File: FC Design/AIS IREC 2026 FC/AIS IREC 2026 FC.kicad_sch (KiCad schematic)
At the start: 52 parts, among them IC1 ADXL314WBCPZ-RL, IC2 MT29F8G08ABACAWP-IT_C_TR, J1 USB4216-03-A, J2 EBAA-02-C, J3 Conn_01x08, J4 EBAA-02-C, J5 EBAA-02-C, J6 USB4216-03-A, Q1 MMBT3906-TP, Q2 DMN2008LFU-7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

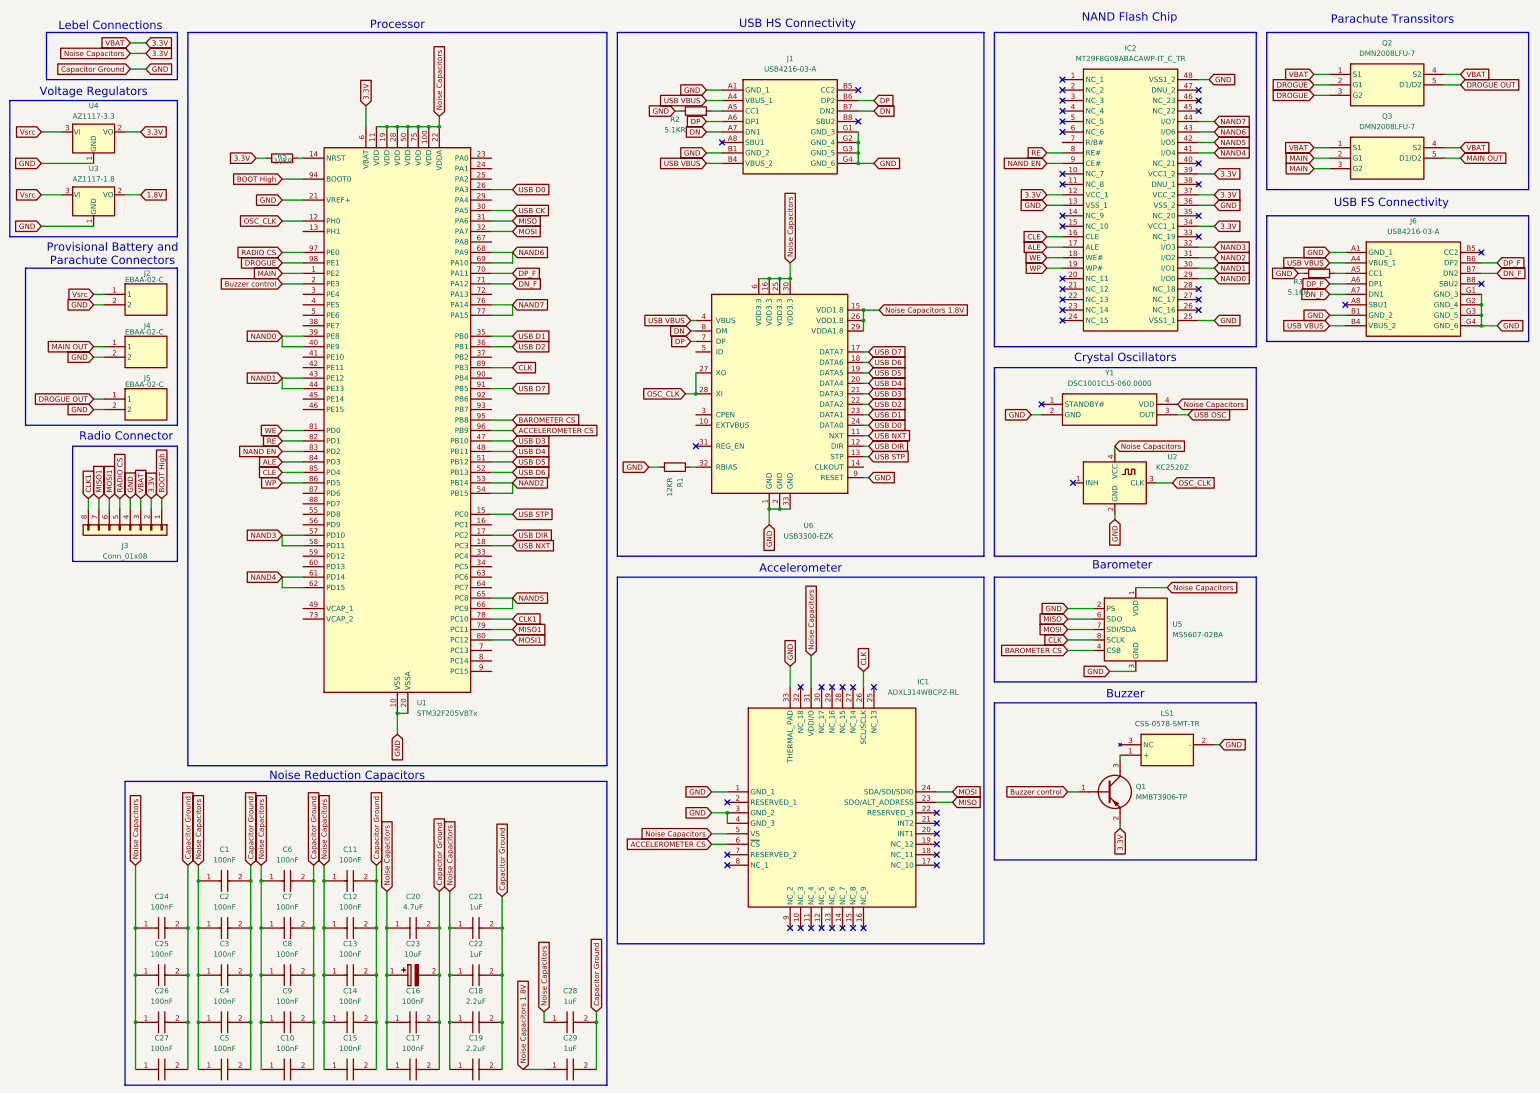
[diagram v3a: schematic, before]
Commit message: Component placement done for pcb
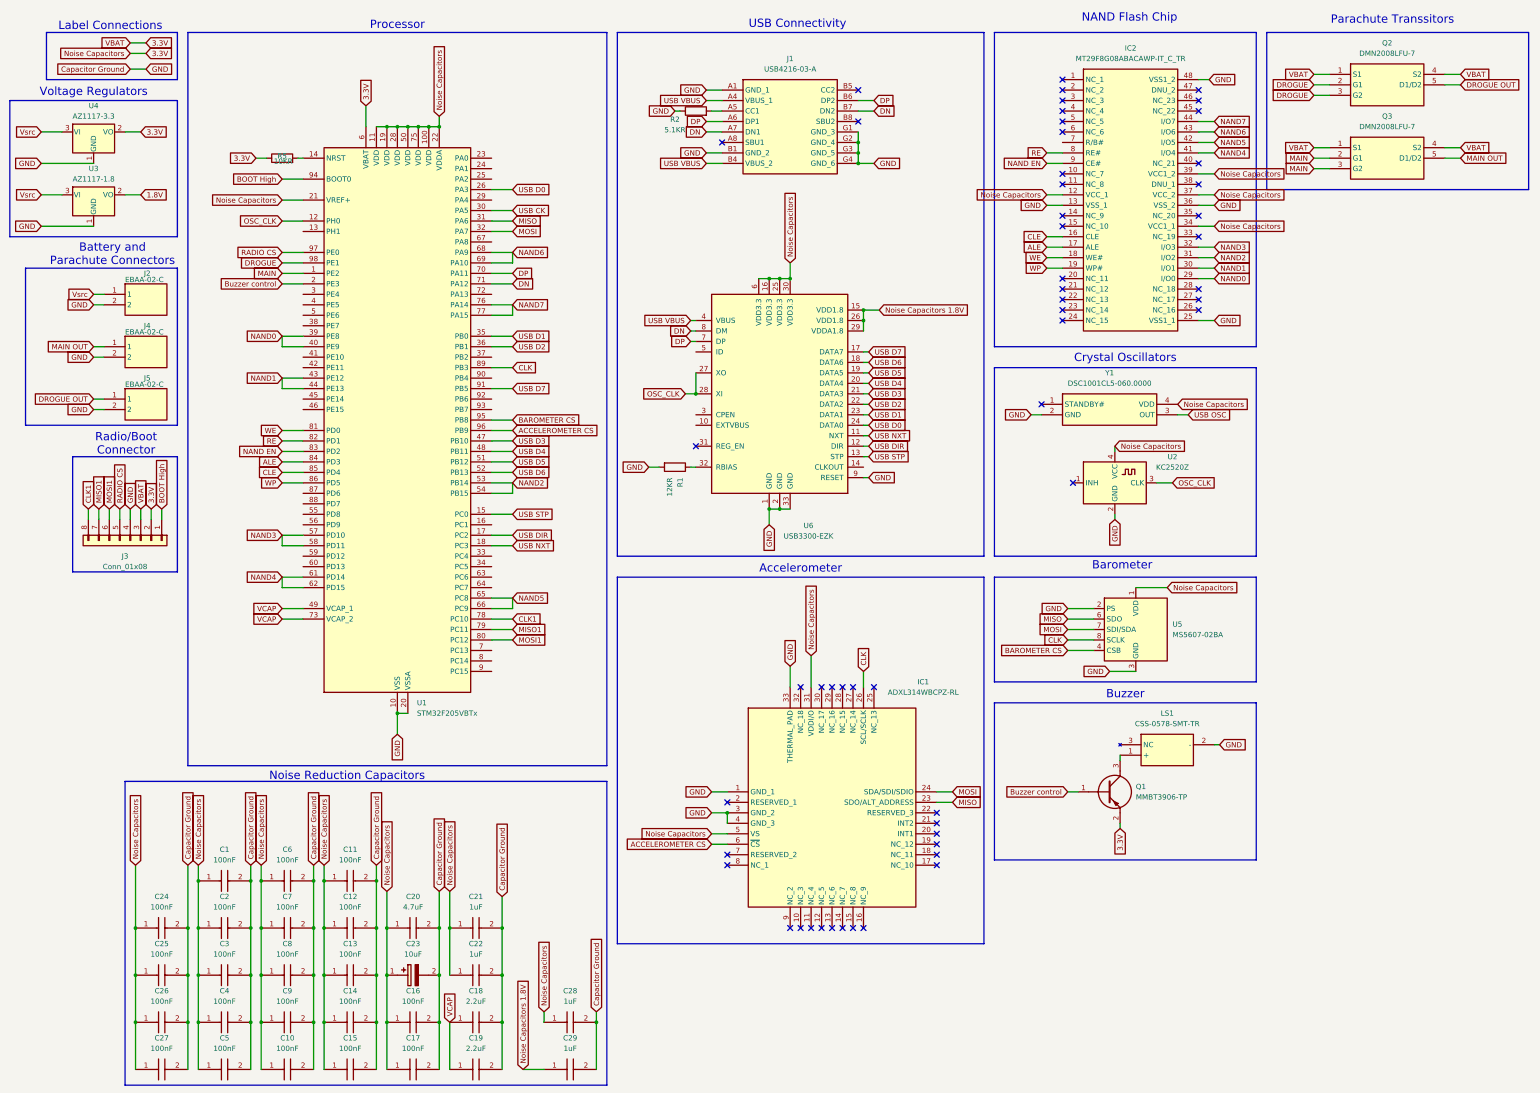
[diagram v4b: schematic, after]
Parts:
- removed J6: USB4216-03-A, SamacSys_Parts:USB421603A, symbol SamacSys_Parts:USB4216-03-A
- removed R3: 5.1KR, Resistor_SMD:R_0201_0603Metric, symbol Device:R
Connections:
- net DN_F is gone; now on net DN: U1.71 (PA12)
- net DP_F is gone; now on net DP: U1.70 (PA11)
- net 3.3V: now also U1.21 (VREF+); no longer C18.1, C19.1
- net Capacitor Ground: no longer U1.21 (VREF+)
- net VCAP: now reaches U1.49 (VCAP_1)
- net VCAP: now also C18.1, C19.1, U1.73 (VCAP_2)
- no-connect marks 57 -> 54
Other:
- note added: "Battery and Parachute Connectors"
- note added: "Label Connections"
- note added: "Radio/Boot Connector"
- note added: "USB Connectivity"
- note removed: "Lebel Connections"
- note removed: "Provisional Battery and Parachute Connectors"
- note removed: "Radio Connector"
- note removed: "USB FS Connectivity"
- note removed: "USB HS Connectivity"
- moved on the sheet: J3

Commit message: Updates to pcb
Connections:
- net Noise Capacitors 1.8V is gone; now on net 1.8V: C29.1, U6.15 (VDD1.8), U6.26 (VDD1.8), U6.29 (VDDA1.8)
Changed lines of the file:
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@@
 	(wire
 		(pts
+			(xy 49.53 27.94) (xy 53.34 27.94)
+		)
+		(stroke
+			(width 0)
+			(type default)
+		)
+	)
+	(wire
+		(pts
 			(xy 137.16 83.82) (xy 142.24 83.82)
 		)
@@
 	(wire
 		(pts
-			(xy 49.53 27.94) (xy 53.34 27.94)
+			(xy 49.53 25.4) (xy 53.34 25.4)
 		)
 		(stroke
@@
 	)
 	(rectangle
-		(start 29.21 25.4)
+		(start 29.21 24.13)
 		(end 60.96 36.83)
 		(stroke
@@
 	(text "Label Connections"
 		(exclude_from_sim no)
-		(at 44.704 23.876 0)
+		(at 44.704 22.352 0)
 		(effects
 			(font
@@
 		)
 	)
+	(global_label "Noise Capacitors 1.8V"
+		(shape input)
+		(at 49.53 27.94 180)
+		(fields_autoplaced yes)
+		(effects
+			(font
+				(size 1.27 1.27)
+			)
+			(justify right)
+		)
+		(property "Intersheetrefs" "${INTERSHEET_REFS}"
+			(at 25.1968 27.94 0)
+			(effects
+				(font
+					(size 1.27 1.27)
+				)
+				(justify right)
+				(hide yes)
+			)
+		)
+	)
 	(global_label "Noise Capacitors"
 		(shape input)
@@
 	(global_label "3.3V"
 		(shape input)
-		(at 53.34 27.94 0)
+		(at 53.34 25.4 0)
 		(fields_autoplaced yes)
 		(effects
@@
 		)
 		(property "Intersheetrefs" "${INTERSHEET_REFS}"
-			(at 60.4376 27.94 0)
+			(at 60.4376 25.4 0)
 			(effects
 				(font
@@
 	(global_label "VBAT"
 		(shape input)
-		(at 49.53 27.94 180)
+		(at 49.53 25.4 180)
 		(fields_autoplaced yes)
 		(effects
@@
 		)
 		(property "Intersheetrefs" "${INTERSHEET_REFS}"
-			(at 42.13 27.94 0)
+			(at 42.13 25.4 0)
 			(effects
 				(font
@@
 			(effects
 				(font
+					(size 1.27 1.27)
+				)
+				(justify left)
+				(hide yes)
+			)
+		)
+	)
+	(global_label "1.8V"
+		(shape input)
+		(at 53.34 27.94 0)
+		(fields_autoplaced yes)
+		(effects
+			(font
+				(size 1.27 1.27)
+			)
+			(justify left)
+		)
+		(property "Intersheetrefs" "${INTERSHEET_REFS}"
+			(at 60.4376 27.94 0)
+			(effects
+				(font
